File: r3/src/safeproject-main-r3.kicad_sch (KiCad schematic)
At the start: 27 parts, among them T1 , T3 , T4 , T5 , T6 , T7 , U1 74LVC1G07DCK

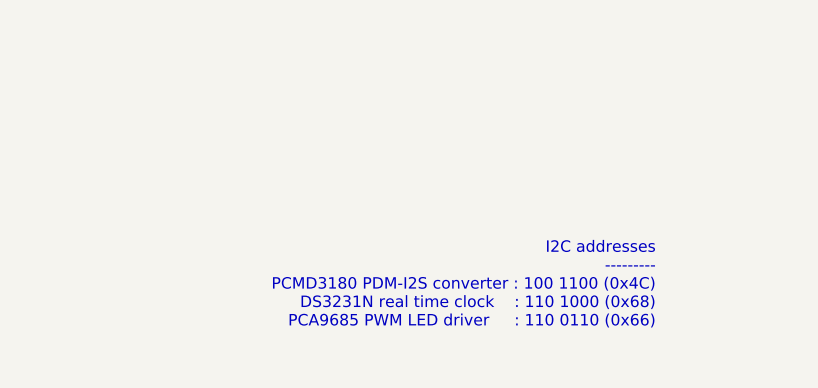
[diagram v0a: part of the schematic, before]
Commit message: Replace LED driver with PCF8574 IO expander. There was some weird interference between the LED PWM signals and the I2S bus, plus the stupid thing initialised with the LED's full white.
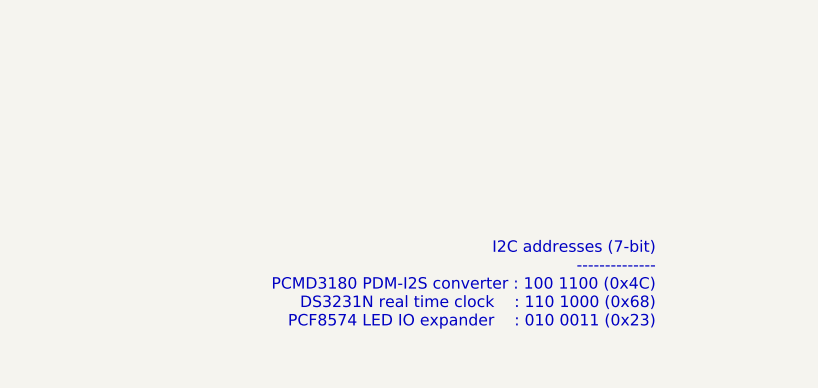
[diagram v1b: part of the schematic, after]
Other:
- note added: "I2C addresses (7-bit) -------------- PCMD3180 PDM-I2S converter : 100 1100 (0x4C) DS3231N real time clock : 110 1000 (0x68) PCF8574 LED IO expander : 010 0011 (0x23)"
- note removed: "I2C addresses --------- PCMD3180 PDM-I2S converter : 100 1100 (0x4C) DS3231N real time clock : 110 1000 (0x68) PCA9685 PWM LED driver : 110 0110 (0x66)"
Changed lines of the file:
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@@
     (effects (font (size 1.27 1.27)) (justify right bottom))
   )
-  (text "I2C addresses\n---------\nPCMD3180 PDM-I2S converter : 100 1100 (0x4C)\nDS3231N real time clock    : 110 1000 (0x68)\nPCA9685 PWM LED driver     : 110 0110 (0x66)\n"
+  (text "I2C addresses (7-bit)\n--------------\nPCMD3180 PDM-I2S converter : 100 1100 (0x4C)\nDS3231N real time clock    : 110 1000 (0x68)\nPCF8574 LED IO expander    : 010 0011 (0x23)\n"
     (at 274.32 270.51 0)
     (effects (font (size 1.27 1.27)) (justify right bottom))
@@
       (reference "#PWR0112") (unit 1) (value "GND") (footprint "")
     )
-    (path "/676be2e4-179b-4538-a96d-4073cd6b4d31/2dea9972-12ec-4eca-a10a-47e0f4c3fe37"
-      (reference "#PWR0113") (unit 1) (value "+3V3") (footprint "")
-    )
     (path "/676be2e4-179b-4538-a96d-4073cd6b4d31/77c42c80-fa99-494d-bee1-81e7261076a1"
       (reference "#PWR0114") (unit 1) (value "+3V3") (footprint "")
     )
-    (path "/676be2e4-179b-4538-a96d-4073cd6b4d31/1f817d31-56b2-41b4-9174-8a40bc70bd59"
-      (reference "#PWR0115") (unit 1) (value "GND") (footprint "")
-    )
     (path "/676be2e4-179b-4538-a96d-4073cd6b4d31/7f4127d3-ac81-4be1-a169-0c2560c4850b"
       (reference "#PWR0116") (unit 1) (value "+3V3") (footprint "")
@@
       (reference "R32") (unit 1) (value "1k") (footprint "Resistor_SMD:R_0603_1608Metric")
     )
-    (path "/676be2e4-179b-4538-a96d-4073cd6b4d31/641ec35e-c0cc-4e68-9f40-c75eaa0324bb"
-      (reference "R33") (unit 1) (value "100k") (footprint "Resistor_SMD:R_0603_1608Metric")
-    )
     (path "/01f77c52-1b52-4742-808d-d7be12bf5723"
       (reference "R34") (unit 1) (value "1k") (footprint "Resistor_SMD:R_0603_1608Metric")
@@
       (reference "U16") (unit 1) (value "ESD7004") (footprint "jeffmakes-footprints:USON-10_2.5x1.0mm_P0.5mm")
     )
-    (path "/676be2e4-179b-4538-a96d-4073cd6b4d31/41410602-d37c-47a3-a968-20aee0d383b4"
-      (reference "U17") (unit 1) (value "PCA9685PW") (footprint "Package_SO:TSSOP-28_4.4x9.7mm_P0.65mm")
-    )
-  )
+    (path "/676be2e4-179b-4538-a96d-4073cd6b4d31/051c51f9-56f1-4030-9fbd-9d998eb169a6"
+      (reference "U?") (unit 1) (value "PCF8574PW") (footprint "Package_SO:SSOP-20_4.4x6.5mm_P0.65mm")
+    )
+  )

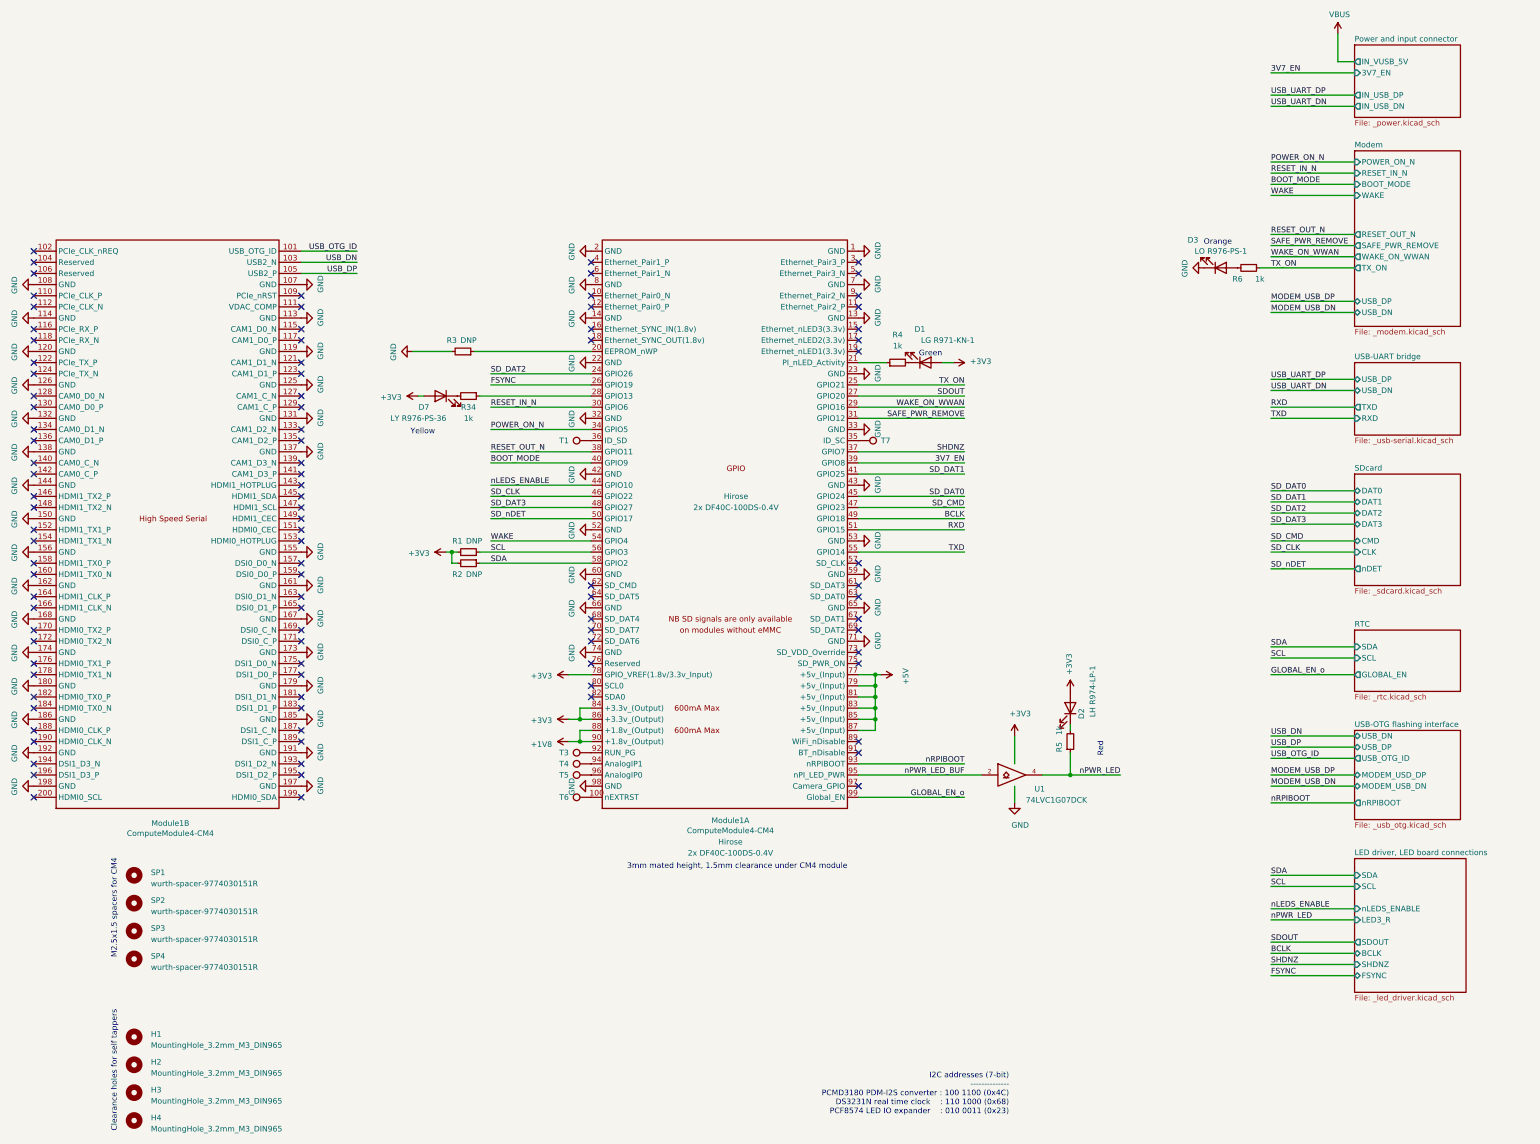
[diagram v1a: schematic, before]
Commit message: Replace fancy level tranlator, which pissed off the modem, with a simple bunch of FETs
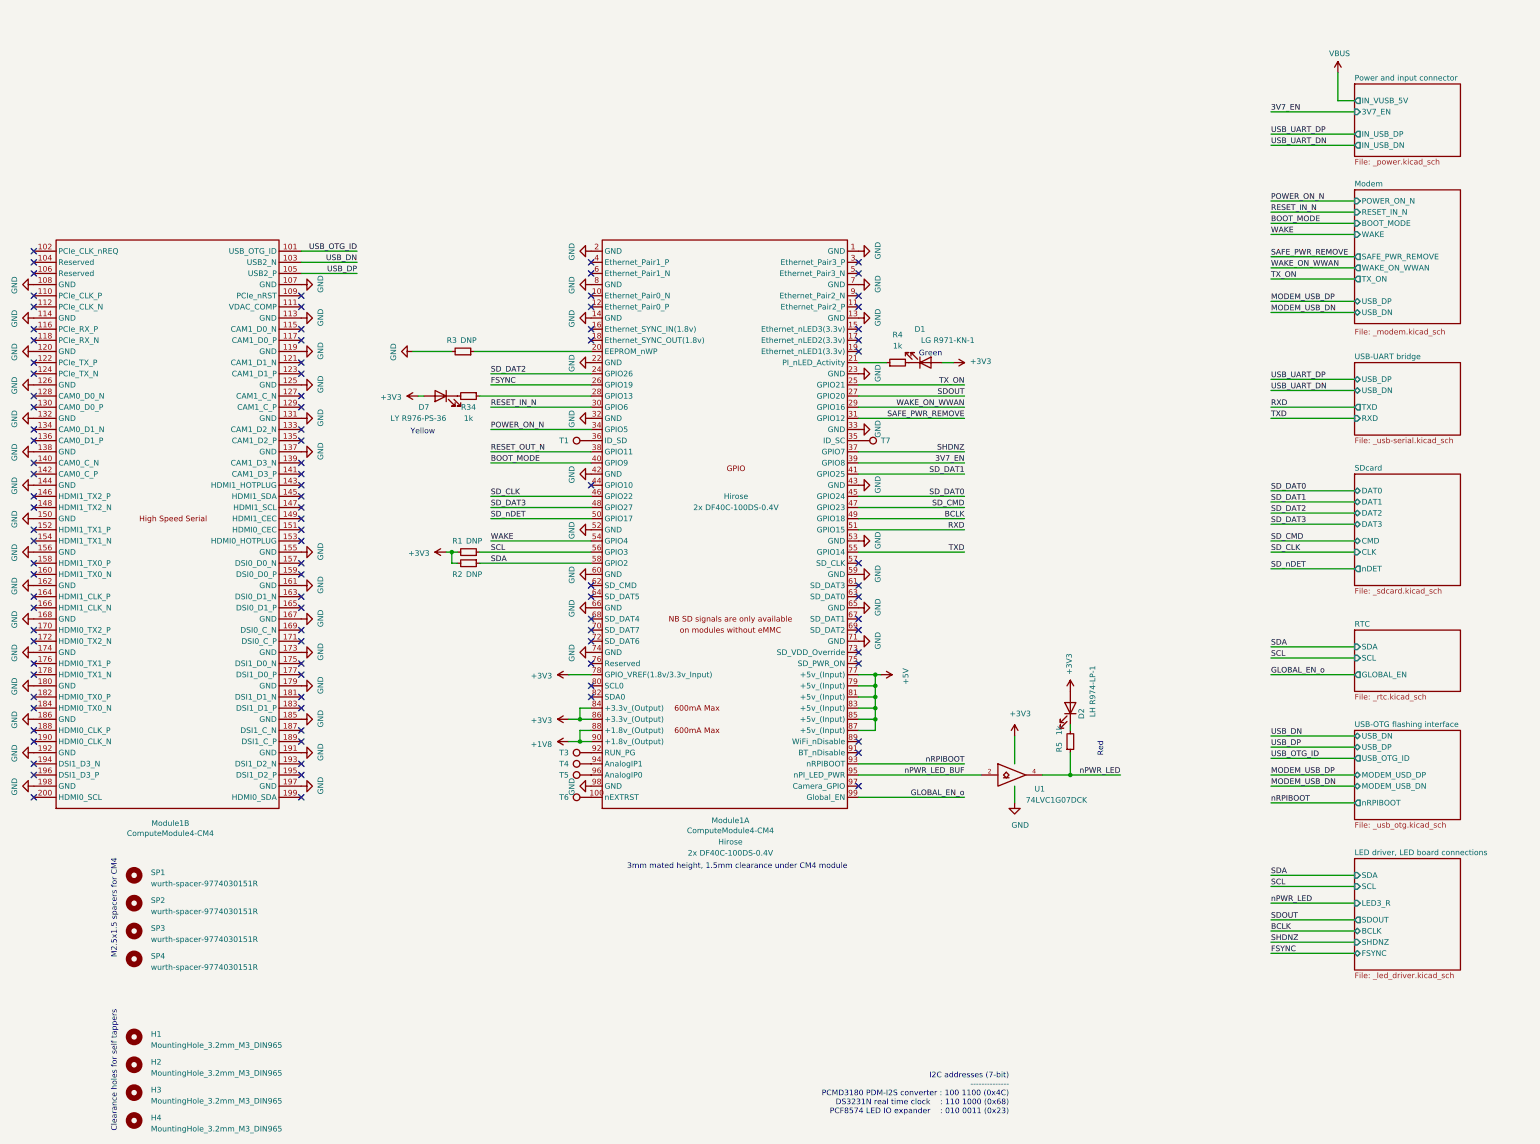
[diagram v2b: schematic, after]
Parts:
- removed D3: LO R976-PS-1, jeffmakes-footprints:CHIPLED-0805, symbol Device:LED
- removed R6: 1k, Resistor_SMD:R_0603_1608Metric, symbol Device:R_Small
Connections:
- net nLEDS_ENABLE: no longer names the net of Module1.44 (GPIO10)
- no-connect marks 98 -> 99
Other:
- sheet LED driver, LED board connections ports: added none; removed nLEDS_ENABLE
- sheet Modem ports: added none; removed RESET_OUT_N
- note removed: "Orange"

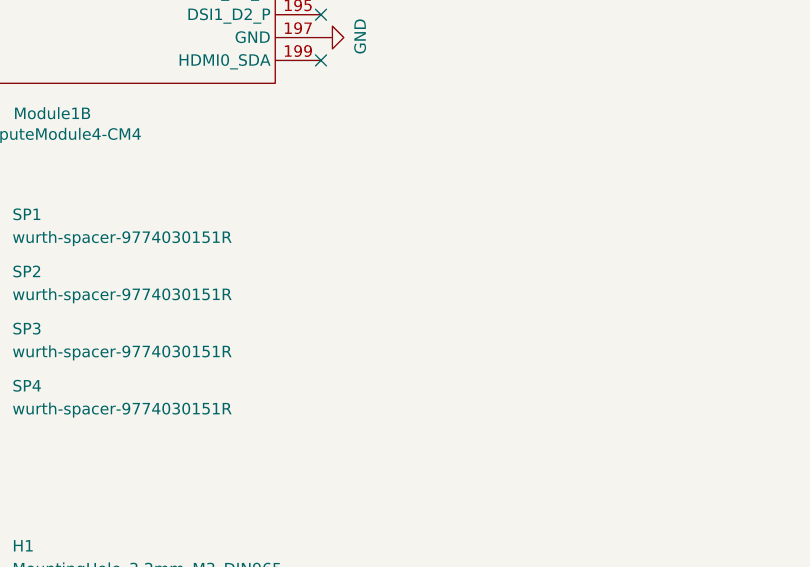
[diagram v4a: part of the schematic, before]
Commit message: Add fiducial symbols
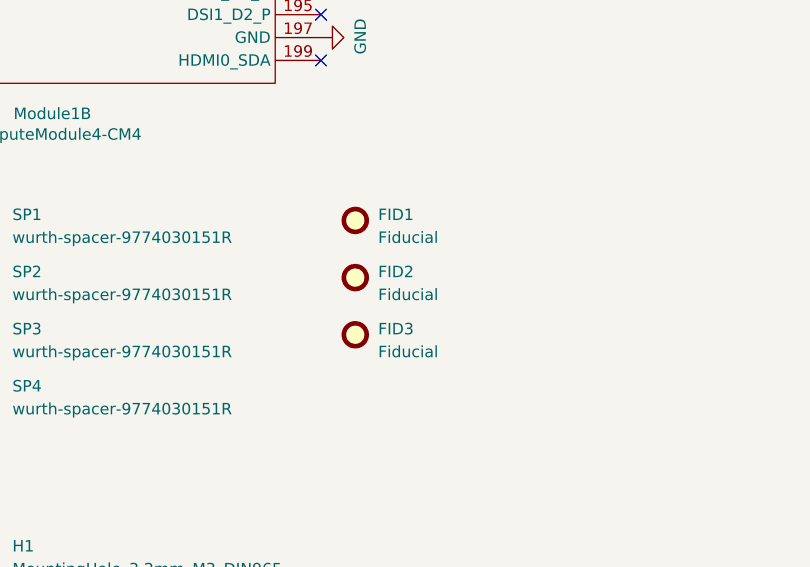
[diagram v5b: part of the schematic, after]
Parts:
- added FID1, FID2, FID3: Fiducial, Fiducial:Fiducial_1mm_Mask2mm, symbol Mechanical:Fiducial

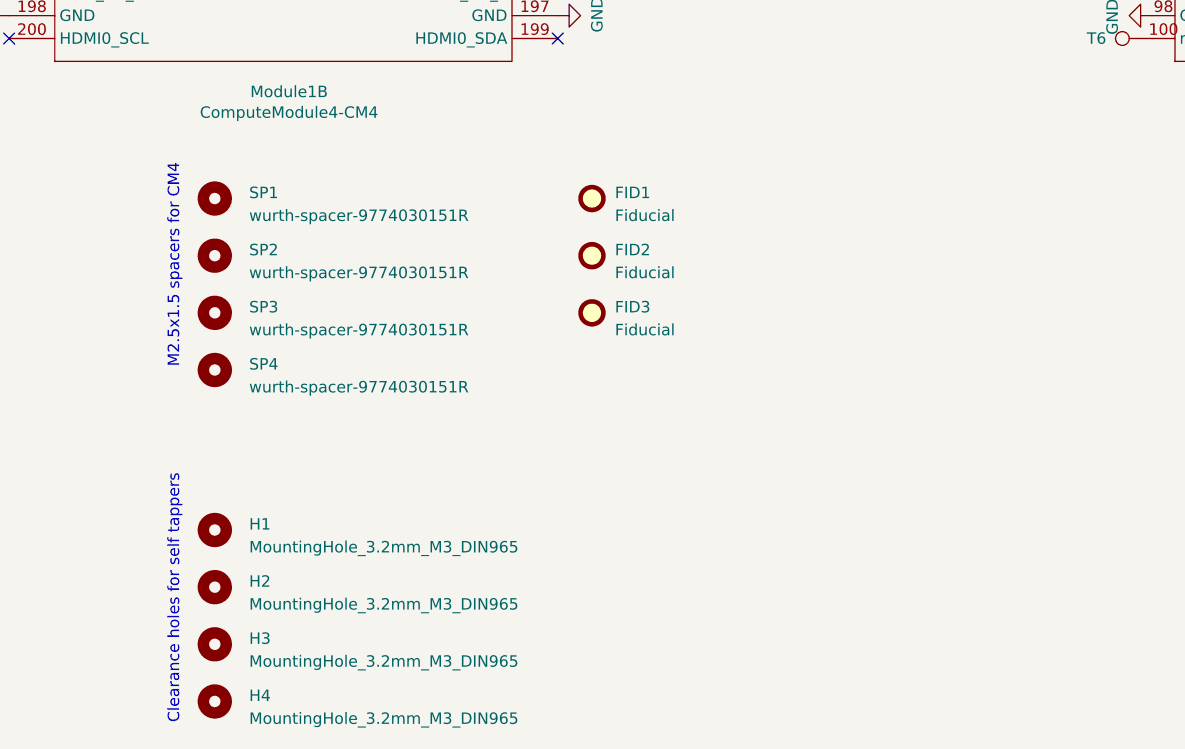
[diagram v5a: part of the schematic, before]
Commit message: Connect Wurth spacer mounting pads to GND
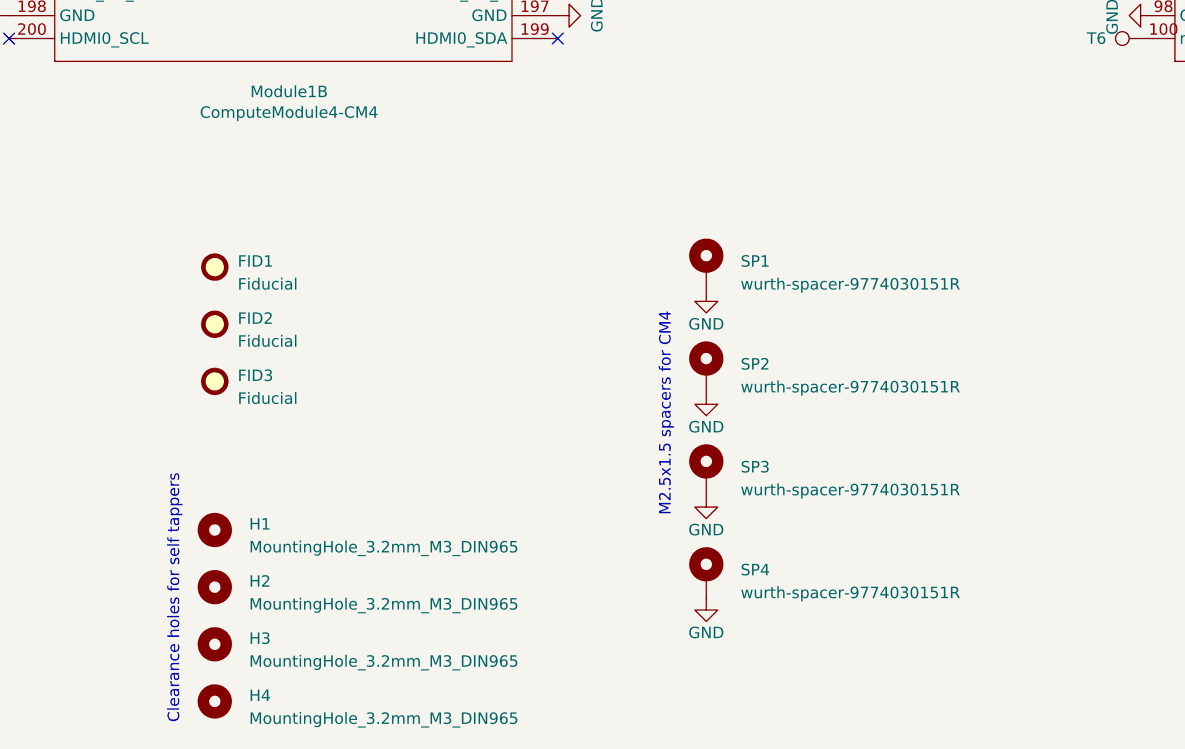
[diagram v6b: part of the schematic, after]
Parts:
- SP1, SP2, SP3, SP4: symbol Mechanical:MountingHole -> Mechanical:MountingHole_Pad
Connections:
- net GND: now also SP1.1, SP2.1, SP3.1, SP4.1
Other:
- moved on the sheet: FID1, FID2, FID3
